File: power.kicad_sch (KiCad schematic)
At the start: 22 parts, among them IC3 CH224K, J5 USB_C_Receptacle_USB2.0, J6 Barrel_Jack, U13 TPD2EUSB30, U20 TPS5430DDA, U9 AMS1117-3.3

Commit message: Increase input voltage range to 10-35V
See #52
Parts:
- L14: value 15uH -> 22uH; footprint Inductor_SMD:L_Sunlord_SWPA4018S -> Inductor_SMD:L_Sunlord_SWPA5040S; LCSC C2846190 -> C68434
- R68: value 6.2k -> 10k; LCSC C4260 -> C25804
- R69: value 2k -> 3.24k; LCSC C22975 -> C22994
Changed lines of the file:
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@@
 			)
 		)
-		(property "Value" "6.2k"
+		(property "Value" "10k"
 			(at 90.17 172.7201 0)
 			(effects
@@
 			)
 		)
-		(property "LCSC" "C4260"
+		(property "LCSC" "C25804"
 			(at 92.71 173.99 0)
 			(effects
@@
 			)
 		)
-		(property "Value" "2k"
+		(property "Value" "3.24k"
 			(at 90.932 180.086 0)
 			(effects
@@
 			)
 		)
-		(property "LCSC" "C22975"
+		(property "LCSC" "C22994"
 			(at 92.71 181.61 0)
 			(effects
@@
 			)
 		)
-		(property "Value" "15uH"
+		(property "Value" "22uH"
 			(at 86.36 166.37 90)
 			(effects
@@
 			)
 		)
-		(property "Footprint" "Inductor_SMD:L_Sunlord_SWPA4018S"
+		(property "Footprint" "Inductor_SMD:L_Sunlord_SWPA5040S"
 			(at 86.36 168.91 0)
 			(effects
@@
 			)
 		)
-		(property "Description" "AMWPH4018S150MT"
+		(property "Description" "SWPA5040S220MT"
 			(at 86.36 168.91 0)
 			(effects
@@
 			)
 		)
-		(property "LCSC" "C2846190"
+		(property "LCSC" "C68434"
 			(at 86.36 168.91 90)
 			(effects

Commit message: Increase size of inductor L14 to allow more power on the 5V rail
See #52
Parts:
- L14: footprint Inductor_SMD:L_Sunlord_SWPA5040S -> Inductor_SMD:L_Sunlord_SWPA8040S; LCSC C68434 -> C334252
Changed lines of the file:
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@@
 			)
 		)
-		(property "Footprint" "Inductor_SMD:L_Sunlord_SWPA5040S"
+		(property "Footprint" "Inductor_SMD:L_Sunlord_SWPA8040S"
 			(at 86.36 168.91 0)
 			(effects
@@
 			)
 		)
-		(property "LCSC" "C68434"
+		(property "LCSC" "C334252"
 			(at 86.36 168.91 90)
 			(effects
 				(font
-					(size 1.27 1.27)
-				)
-				(hide yes)
-			)
-		)
-		(property "LCSC alt" ""
-			(at 86.36 168.91 0)
-			(effects
-				(font

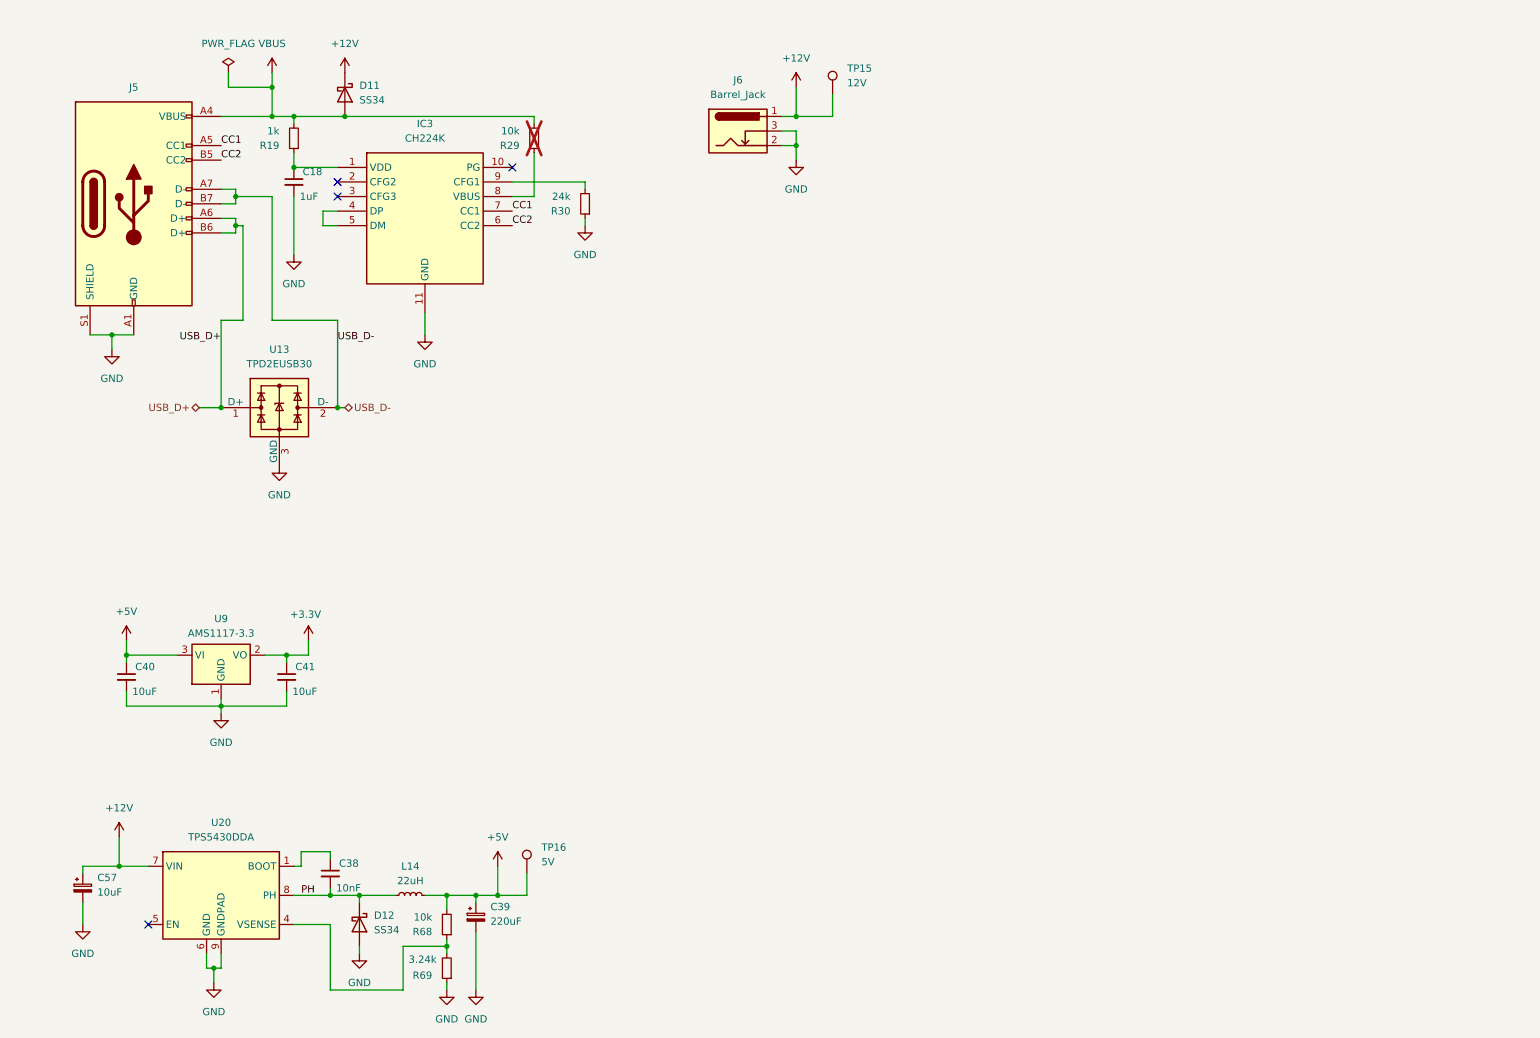
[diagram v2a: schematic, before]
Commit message: Add Reverse polarity protection
Closes #55
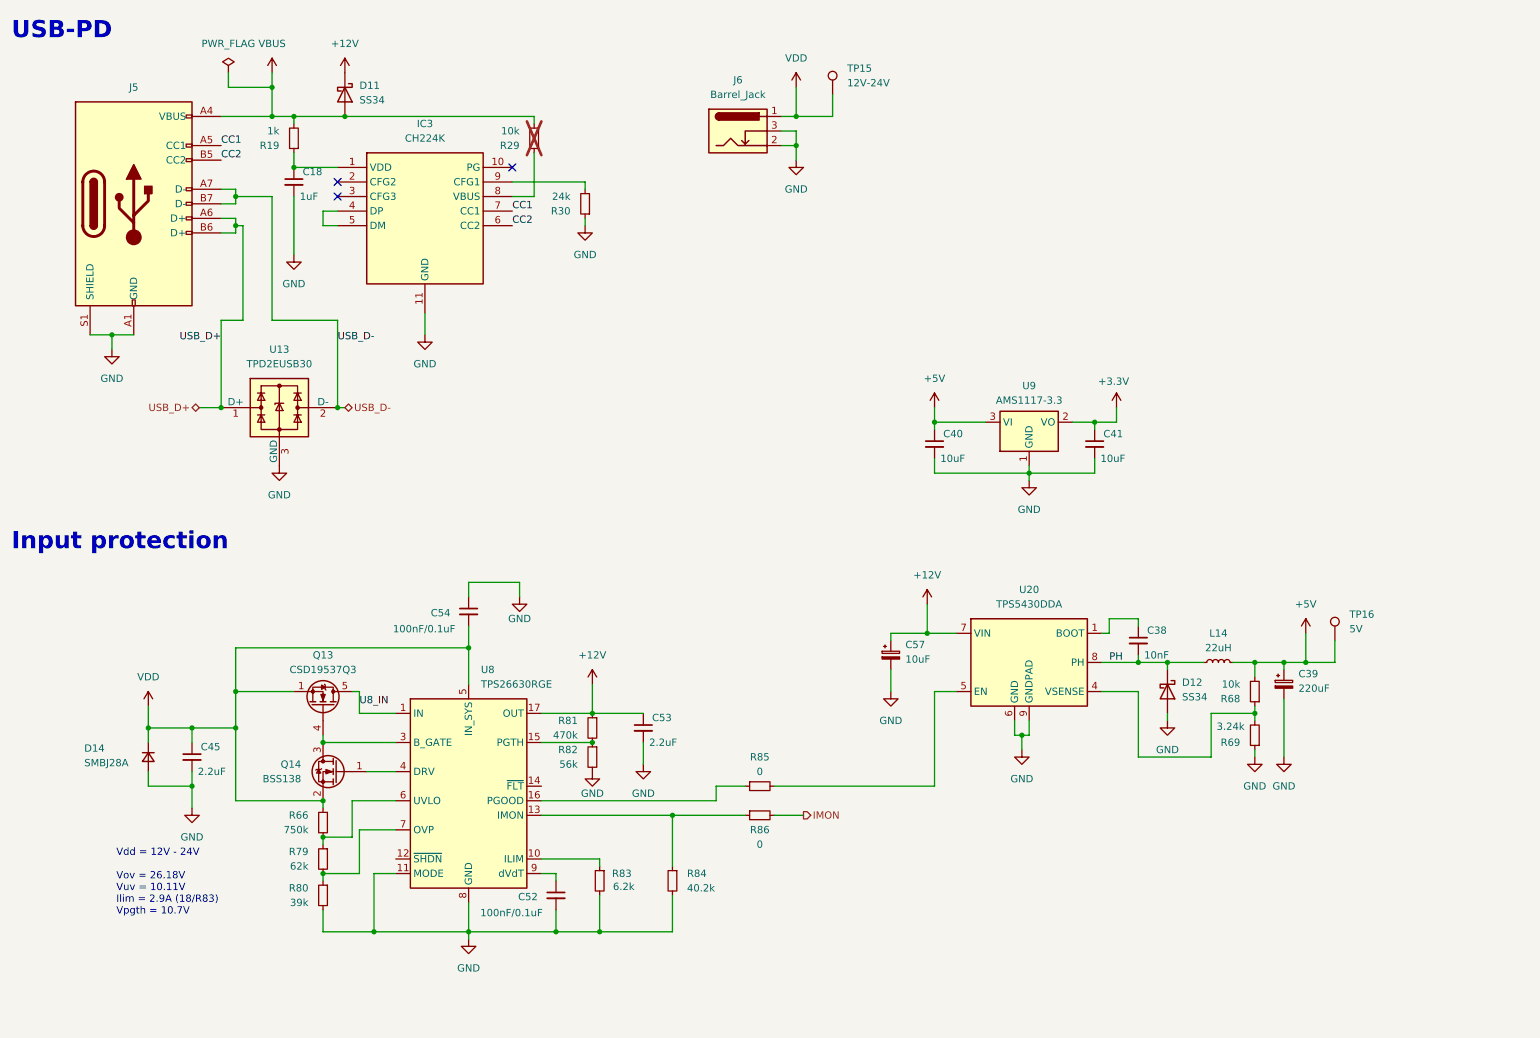
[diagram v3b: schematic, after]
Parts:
- added C45, C53: 2.2uF, Capacitor_SMD:C_1206_3216Metric, symbol Device:C_Small
- added C52, C54: 100nF/0.1uF, Capacitor_SMD:C_0402_1005Metric, symbol Device:C_Small
- added D14: SMBJ28A, Diode_SMD:D_SMB, symbol Device:D_Small
- added Q13: CSD19537Q3, Package_SON:VSON-8_3.3x3.3mm_P0.65mm_NexFET, symbol Transistor_FET:CSD19537Q3
- added Q14: BSS138, Package_TO_SOT_SMD:SOT-23, symbol Transistor_FET:BSS138
- added R66: 750k, Resistor_SMD:R_0603_1608Metric, symbol Device:R_Small
- added R79: 62k, Resistor_SMD:R_0603_1608Metric, symbol Device:R_Small
- added R80: 39k, Resistor_SMD:R_0402_1005Metric, symbol Device:R_Small
- added R81: 470k, Resistor_SMD:R_0603_1608Metric, symbol Device:R_Small
- added R82: 56k, Resistor_SMD:R_0603_1608Metric, symbol Device:R_Small
- added R83: 6.2k, Resistor_SMD:R_0603_1608Metric, symbol Device:R_Small
- added R84: 40.2k, Resistor_SMD:R_0603_1608Metric, symbol Device:R_Small
- added R85, R86: 0, Resistor_SMD:R_0402_1005Metric, symbol Device:R_Small
- added U8: TPS26630RGE, Package_DFN_QFN:Texas_RGE0024H_VQFN-24-1EP_4x4mm_P0.5mm_EP2.7x2.7mm_ThermalVias, symbol Power_Management:TPS26630RGE
- TP15: value 12V -> 12V-24V
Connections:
- net +12V: now also C53.1, R81.1, U8.17 (OUT), U8.18 (OUT); no longer J6.1, TP15.1
- net GND: now also C45.2, C52.2, C53.2, C54.1, D14.2 (A), R80.2, R82.2, R83.2, R84.2, U8.11 (MODE), U8.25 (GND), U8.8 (GND)
- net at U20.5 (EN): now also R85.2
- new net: R85.1, U8.16 (PGOOD)
- new net: R83.1, U8.10 (ILIM)
- new net: R84.1, R86.1, U8.13 (IMON)
- new net: R81.2, R82.1, U8.15 (PGTH)
- new net: Q13.4 (G), Q14.3 (D), U8.3 (B_GATE)
- new net: Q14.1 (G), U8.4 (DRV)
- new net: R66.2, R79.1, U8.6 (UVLO)
- new net: R79.2, R80.1, U8.7 (OVP)
- new net: C52.1, U8.9 (dVdT)
- new net IMON: R86.2
- new net U8_IN: Q13.5 (D), U8.1 (IN), U8.2 (IN)
- new net VDD: C45.1, C54.2, D14.1 (K), J6.1, Q13.1 (S), Q13.2 (S), Q13.3 (S), Q14.2 (S), R66.1, TP15.1, U8.5 (IN_SYS)
- no-connect marks 4 -> 3
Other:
- note added: "Input protection"
- note added: "USB-PD"
- note added: "Vdd = 12V - 24V Vov = 26.18V Vuv = 10.11V Ilim = 2.9A (18/R83) Vpgth = 10.7V"
- moved on the sheet: C38, C39, C40, C41, C57, D12, L14, R68, R69, TP16, U20, U9

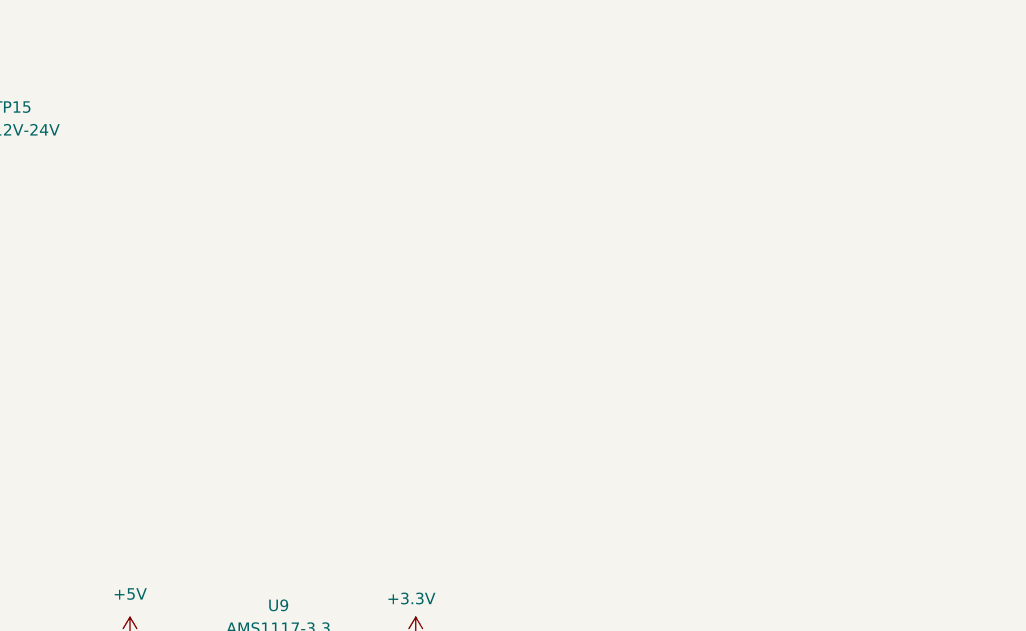
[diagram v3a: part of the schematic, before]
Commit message: Protect CAN connector from over voltage
Closes #57
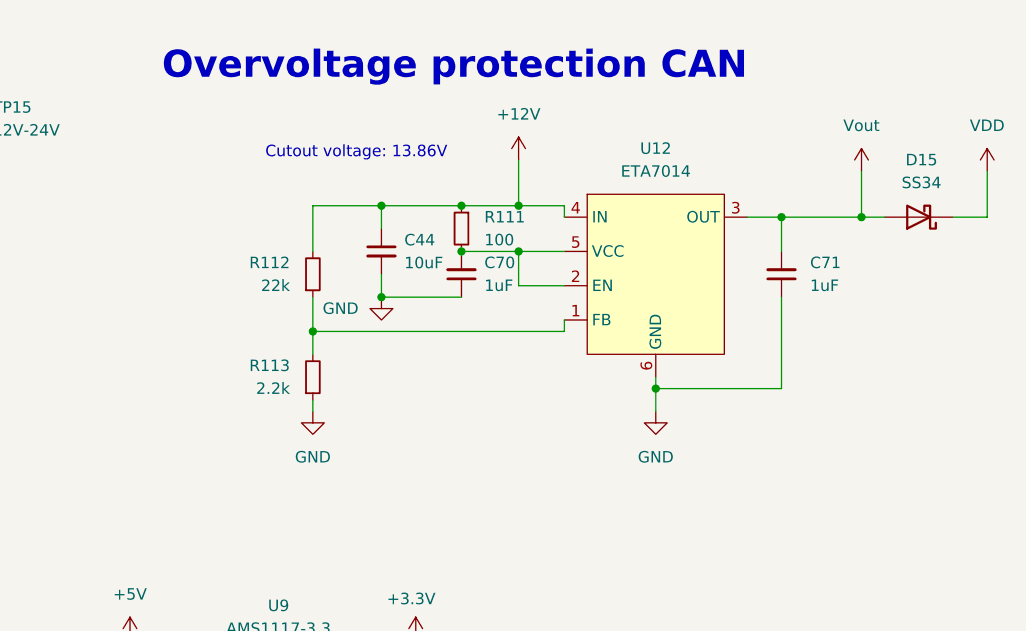
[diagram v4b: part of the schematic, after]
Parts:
- added C44: 10uF, Capacitor_SMD:C_0603_1608Metric, symbol Device:C_Small
- added C70, C71: 1uF, Capacitor_SMD:C_0603_1608Metric, symbol Device:C_Small
- added D15: SS34, Diode_SMD:D_SMA, symbol Diode:SS34
- added R111: 100, Resistor_SMD:R_0402_1005Metric, symbol Device:R_Small
- added R112: 22k, Resistor_SMD:R_0402_1005Metric, symbol Device:R_Small
- added R113: 2.2k, Resistor_SMD:R_0402_1005Metric, symbol Device:R_Small
- added U12: ETA7014, Package_TO_SOT_SMD:SOT-23-6, symbol HydroponicFlowerControl:ETA7014S2G
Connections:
- net +12V: now also C44.1, R111.1, R112.2, U12.4 (IN)
- net GND: now also C44.2, C70.1, C71.1, R113.1, U12.6 (GND)
- net VDD: now also D15.1 (K)
- new net: R112.1, R113.2, U12.1 (FB)
- new net: C70.2, R111.2, U12.2 (EN), U12.5 (VCC)
- new net Vout: C71.2, D15.2 (A), U12.3 (OUT)
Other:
- note added: "Cutout voltage: 13.86V"
- note added: "Overvoltage protection CAN"

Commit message: Update files to KiCad 10.0
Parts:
- R29: now in the parts list

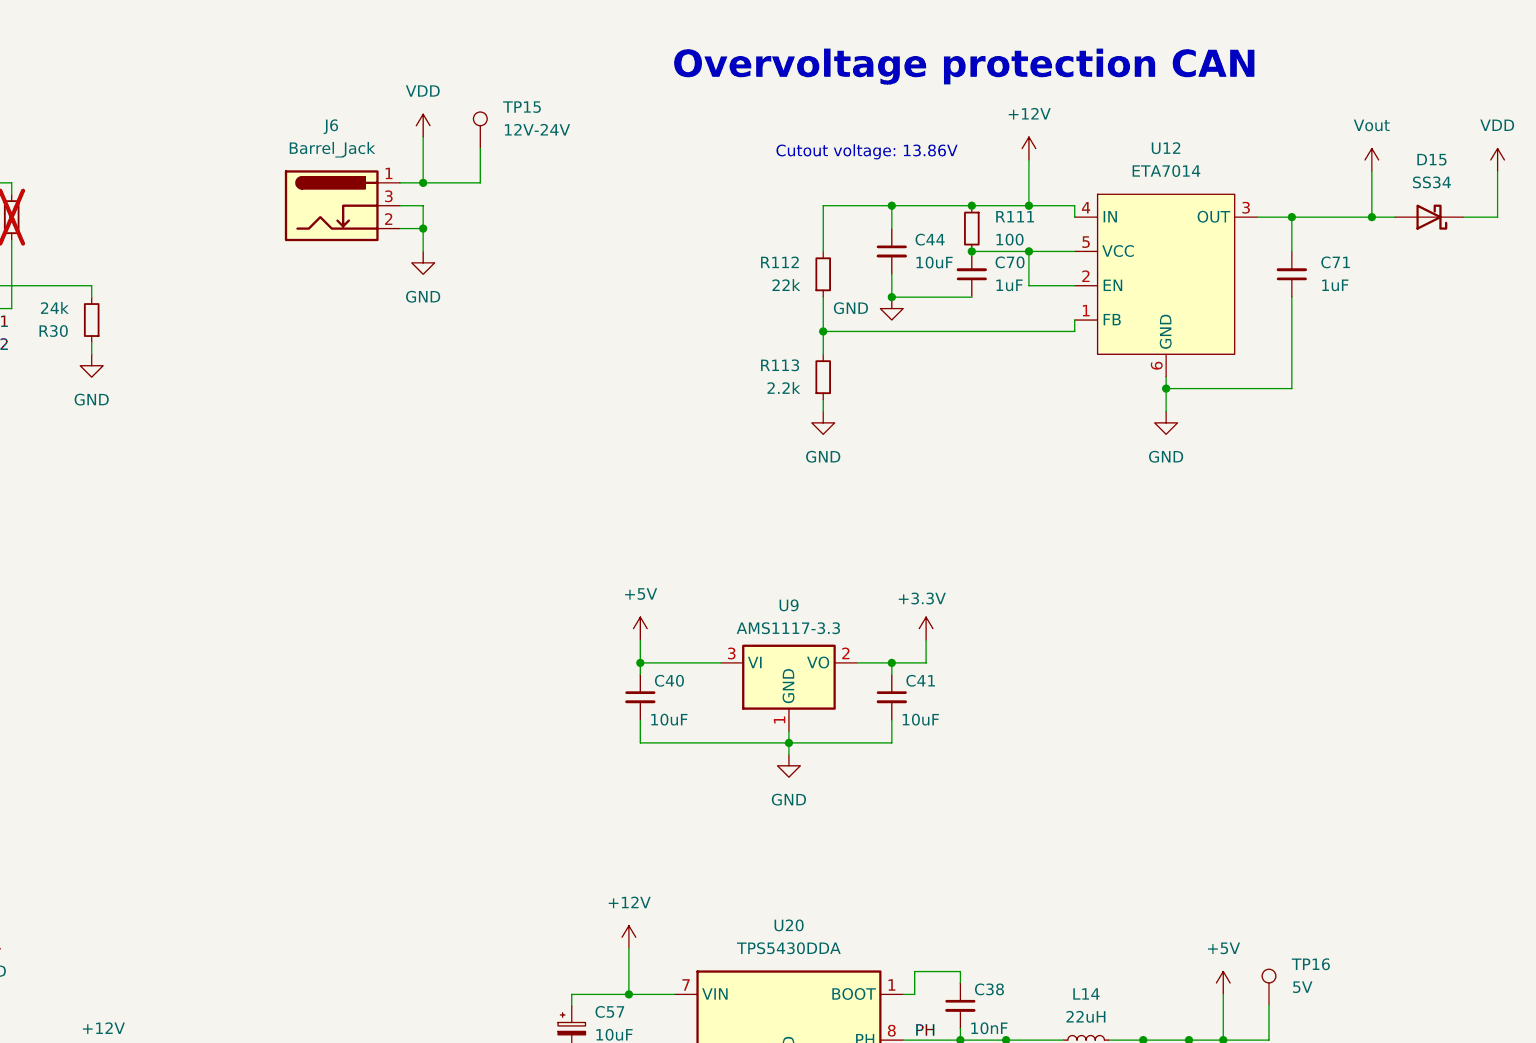
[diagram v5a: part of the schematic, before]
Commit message: Replace diode for Vin from CAN with ideal diode
See #63
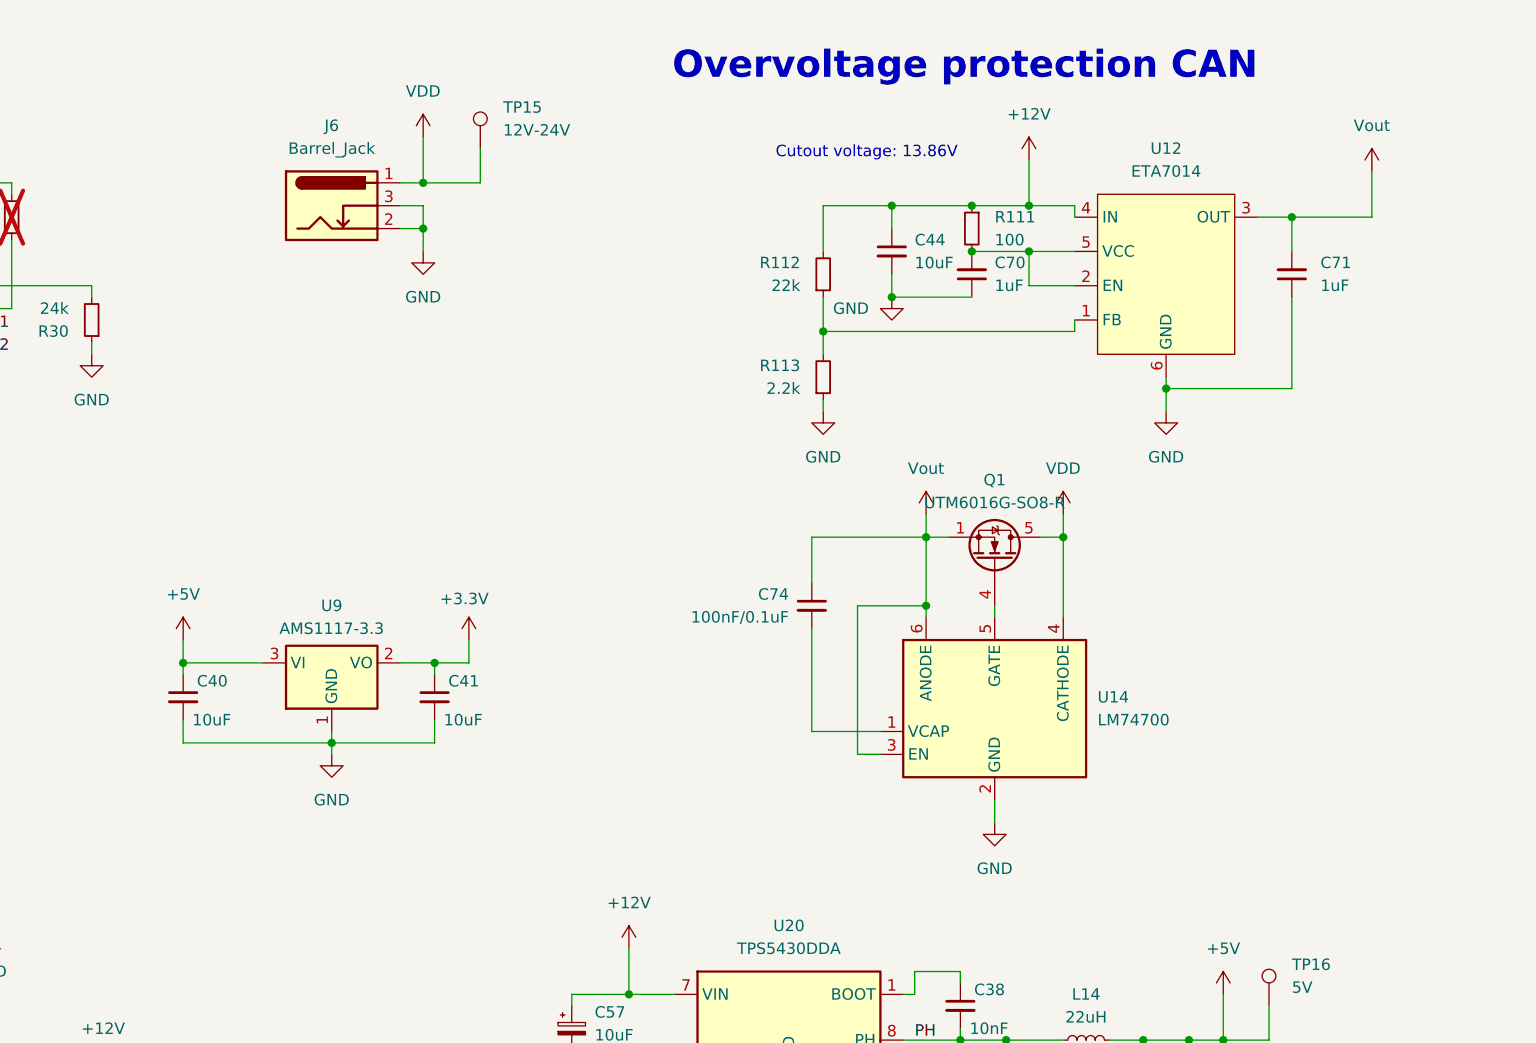
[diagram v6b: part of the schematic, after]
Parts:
- removed D15: SS34, Diode_SMD:D_SMA, symbol Diode:SS34
- added C74: 100nF/0.1uF, Capacitor_SMD:C_0603_1608Metric, symbol Device:C_Small
- added Q1: UTM6016G-SO8-R, Package_SO:SOIC-8_3.9x4.9mm_P1.27mm, symbol Transistor_FET:IRF7403
- added U14: LM74700, Package_TO_SOT_SMD:SOT-23-6, symbol Power_Management:LM74700
- R29: now left out of the parts list
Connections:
- net GND: now also U14.2 (GND)
- net VDD: now also Q1.5 (D), Q1.6 (D), Q1.7 (D), Q1.8 (D), U14.4 (CATHODE)
- net Vout: now also C74.1, Q1.1 (S), Q1.2 (S), Q1.3 (S), U14.3 (EN), U14.6 (ANODE)
- new net: Q1.4 (G), U14.5 (GATE)
- new net: C74.2, U14.1 (VCAP)
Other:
- moved on the sheet: C40, C41, U9
